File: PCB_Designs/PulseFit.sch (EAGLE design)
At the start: 54 parts

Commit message: updates
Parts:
- removed C10, C9: 100n, resistor:C-EUC0402
- removed COMP, VREF: AD8603UJ, analog-devices:AD8603UJ
- removed JST: JST-PTH, Orlando:JST-PTH
- removed LED1, LED10, LED12, LED16, LED2, LED22, LED23, LED24, LED25, LED26, LED28, LED3, LED4, LED6, LED7, LED8, LED9: (no value), SparkFun-LED:LED5MM
- removed PD1, PD2: PD-ODD-900-001, Orlando:PD-ODD-900-001
- removed R6, R7: 49.9k, resistor:R-US_R0402
- added BATT-CR2032: (no value), SparkFun-Electromechanical:BATTERY20SMD
- added C11: 10n, resistor:C-EUC0402
- added LD1, LD10, LD12, LD13, LD14, LD15, LD16, LD17, LD18, LD2, LD3, LD4, LD5, LD6, LD7, LD8, LD9, LED13: LED-LTST-C230KRKT, Orlando:LED-LTST-C230KRKT
- added PD: LED-PD15-22B_TR8, Orlando:LED-PD15-22B_TR8
- C1: value 33n -> 1uF
- C2, C4: value 570n -> 1u
- C3: value 318n -> 10u; device resistor:C-EUC0402 -> resistor:C-EUC0805
- C5: value 318n -> 10n
- C6: device resistor:C-EUC0402 -> resistor:C-EUC0805
- C7: value 100n -> 10n
- C8: value 100n -> 10u; device resistor:C-EUC0402 -> resistor:C-EUC0805
- GAIN: value AD8609RU -> MCP6004
- LED11: value (none) -> LED-LTST-C230KRKT; device SparkFun-LED:LED5MM -> Orlando:LED-LTST-C230KRKT
- POWER: value ON -> SWITCH-DPDT-JS202011JCQN; device SparkFun-LED:LED0603 -> SparkFun-Electromechanical:SWITCH-DPDT-JS202011JCQN
- R1: value 1M -> 32k
- R10: value 100k -> 3.3M
- R11, R5: value 10k -> 32k
- R13: value (none) -> 169
- R14: value 100 -> 1k
- R2: value 1M -> 3.3M
- R3, R8, R9: value 1M -> 1.5M
- R4: value 100k -> 1.5M
- renumbered LED5 to PULSE
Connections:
- removed net 1/2-VDD: R11.1, R5.1, VREF.IN-, VREF.OUT
- removed net N$7: R6.1, R7.2, VREF.IN+
- new net N$11: C11.2, C4.1, GAINB.OUT, R2.2
- new net N$14: C8.2, R5.1
- net ANODE: now also LD1.A, LD10.A, LD12.A, LD13.A, LD14.A, LD15.A, LD16.A, LD17.A, LD18.A, LD2.A, LD3.A, LD4.A, LD5.A, LD6.A, LD7.A, LD8.A, LD9.A; no longer LED1.A, LED10.A, LED12.A, LED16.A, LED2.A, LED22.A, LED23.A, LED24.A, LED25.A, LED26.A, LED28.A, LED3.A, LED4.A, LED6.A, LED7.A, LED8.A, LED9.A
- net COMP: now also BREAKOUT.3, GAIND.OUT; no longer BREAKOUT.1, COMP.OUT
- net GND: now also BATT-CR2032.-, C3.1, C8.1, LD1.C, LD10.C, LD12.C, LD13.C, LD14.C, LD15.C, LD16.C, LD17.C, LD18.C, LD2.C, LD3.C, LD4.C, LD5.C, LD6.C, LD7.C, LD8.C, LD9.C, POWER.4, POWER.5, POWER.6, R4.2; no longer C10.2, C8.2, C9.2, COMP.-VS, GAINA.IN+, JST.-, LED1.C, LED10.C, LED12.C, LED16.C, LED2.C, LED22.C, LED23.C, LED24.C, LED25.C, LED26.C, LED28.C, LED3.C, LED4.C, LED6.C, LED7.C, LED8.C, LED9.C, PD1.+, PD2.+, R3.2, R6.2, VREF.-VS
- net N$1: now also PD.A; no longer PD1.-, PD2.-
- net N$10: now also C11.1, GAINB.IN-, R2.1, R5.2; no longer D1.A, GAIND.IN-, GAIND.OUT
- net N$12: now also LED13.C; no longer POWER.C
- net N$4: now also R3.2, R4.1; no longer R2.2, R3.1
- net N$5: now also BATT-CR2032.+, POWER.2; no longer C3.1, GAINB.IN-, R4.1, R5.2
- net N$6: now also R11.1; no longer C4.1, GAINB.OUT, R4.2
- net PEAK: now also GAIND.IN-; no longer COMP.IN-
- net PULSE: now also BREAKOUT.1, D1.A; no longer BREAKOUT.3, COMP.IN+
- net VCC: now also GAINA.IN+, LED13.A, PD.C, POWER.1, R3.1; no longer C10.1, C8.1, C9.1, COMP.+VS, JST.+, POWER.A, R2.1, R7.1, VREF.+VS
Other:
- note added: "Orlando S. Hoilett @oshoilett @CalvaryEngineering Made in the @IICEPD Creative Commons License Attribution-NonCommercial- ShareAlike 3.0 Unported"
- note added: "PulseFit V.4.0"
- note added: "Threshold Adjuster and Pulse Detector"
- note removed: "1/2 Vcc Generator"
- note removed: "Orlando S. Hoilett Calvary Eng, IICEPD Creative Commons License Attribution-NonCommercial-ShareAlike"
- note removed: "Pulse Detector"
- note removed: "PulseFit V.1.0"
- note removed: "Threshold Adjuster"
- moved on the sheet: BREAKOUT, C2, C3, C4, C6, C7, C8, D1, GAINB, GAIND, GAINP, LED11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

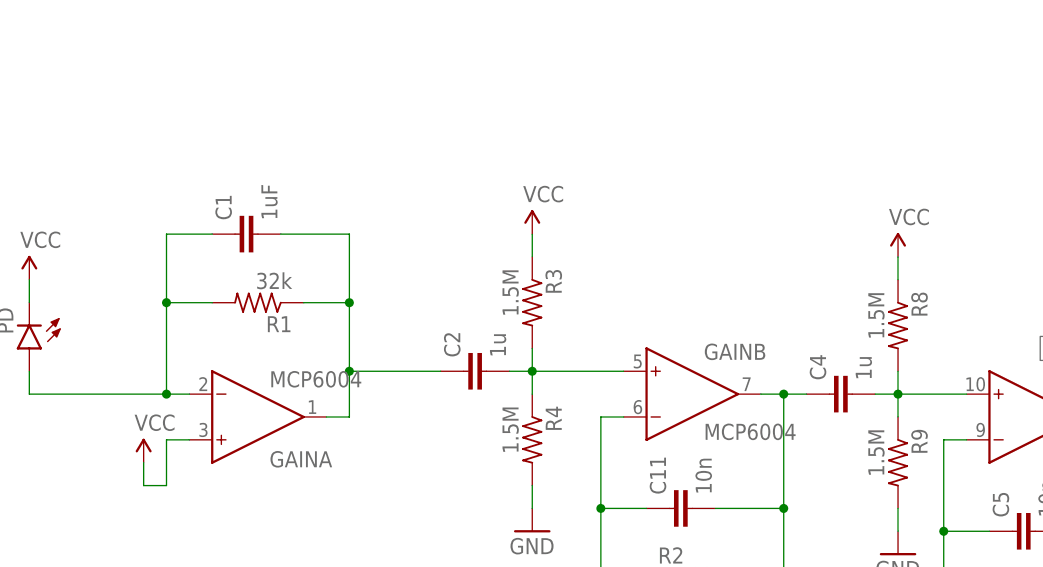
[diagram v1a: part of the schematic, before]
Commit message: updated PulseFit BOM and added disclaimer in schematic
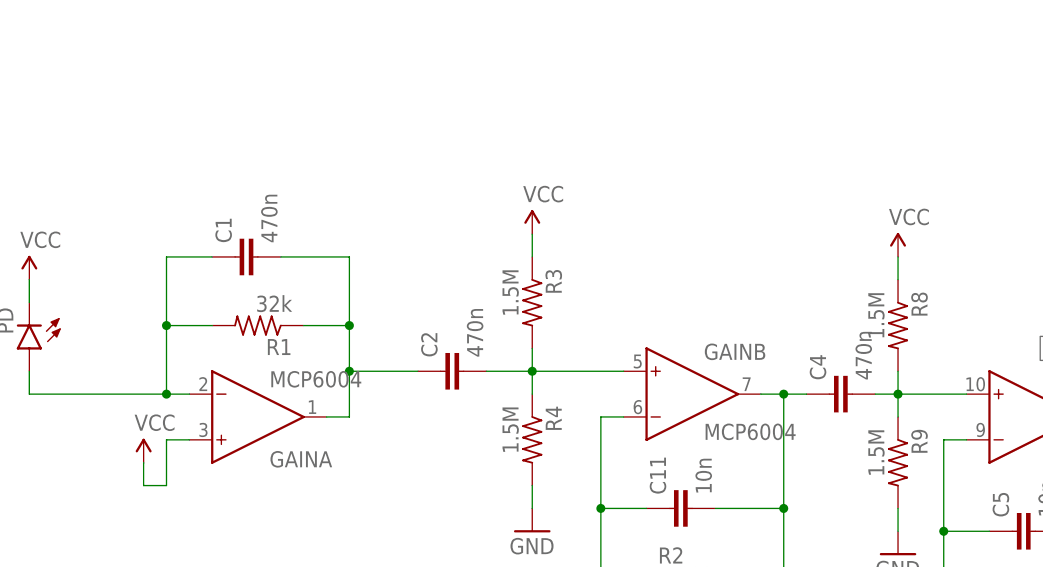
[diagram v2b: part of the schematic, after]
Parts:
- C1: value 1uF -> 470n
- C2, C4: value 1u -> 470n
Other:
- note added: "NOTE: This is NOT a medical device"
- note added: "Orlando S. Hoilett @oshoilett @CalvaryEngineering Made in the @IICEPD Creative Commons License Attribution-NonCommercial- ShareAlike 4.0 Unported"
- note removed: "Orlando S. Hoilett @oshoilett @CalvaryEngineering Made in the @IICEPD Creative Commons License Attribution-NonCommercial- ShareAlike 3.0 Unported"
- moved on the sheet: C1, C2, R1
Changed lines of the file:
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@@
 <?xml version="1.0" encoding="utf-8"?>
 <!DOCTYPE eagle SYSTEM "eagle.dtd">
-<eagle version="7.4.0">
+<eagle version="7.3.0">
 <drawing>
 <settings>
@@
 <parts>
 <part name="GAIN" library="analog-devices" deviceset="AD8609" device="RU" value="MCP6004"/>
-<part name="C1" library="resistor" deviceset="C-EU" device="C0402" value="1uF"/>
+<part name="C1" library="resistor" deviceset="C-EU" device="C0402" value="470n"/>
 <part name="R1" library="resistor" deviceset="R-US_" device="R0402" value="32k"/>
-<part name="C4" library="resistor" deviceset="C-EU" device="C0402" value="1u"/>
+<part name="C4" library="resistor" deviceset="C-EU" device="C0402" value="470n"/>
 <part name="R8" library="resistor" deviceset="R-US_" device="R0402" value="1.5M"/>
 <part name="R9" library="resistor" deviceset="R-US_" device="R0402" value="1.5M"/>
@@
 <part name="C3" library="resistor" deviceset="C-EU" device="C0805" value="10u"/>
 <part name="GND1" library="SparkFun-Aesthetics" deviceset="GND" device=""/>
-<part name="C2" library="resistor" deviceset="C-EU" device="C0402" value="1u"/>
+<part name="C2" library="resistor" deviceset="C-EU" device="C0402" value="470n"/>
 <part name="R3" library="resistor" deviceset="R-US_" device="R0402" value="1.5M"/>
 <part name="R4" library="resistor" deviceset="R-US_" device="R0402" value="1.5M"/>
@@
 Creative Commons License
 Attribution-NonCommercial-
-ShareAlike 3.0 Unported </text>
+ShareAlike 4.0 Unported </text>
 <wire x1="-30.48" y1="147.32" x2="345.44" y2="147.32" width="1.27" layer="94" style="longdash"/>
 <wire x1="345.44" y1="147.32" x2="345.44" y2="-20.32" width="1.27" layer="94" style="longdash"/>
@@
 <wire x1="193.04" y1="88.9" x2="193.04" y2="48.26" width="0.508" layer="90" style="shortdash"/>
 <wire x1="193.04" y1="48.26" x2="139.7" y2="48.26" width="0.508" layer="90" style="shortdash"/>
+<text x="200.66" y="139.7" size="3.81" layer="90">NOTE: This is NOT a medical device</text>
 </plain>
 <instances>
@@
 <instance part="GAIN" gate="D" x="167.64" y="81.28"/>
 <instance part="GAIN" gate="P" x="35.56" y="10.16"/>
-<instance part="C1" gate="G$1" x="35.56" y="96.52" rot="R90"/>
-<instance part="R1" gate="G$1" x="38.1" y="88.9" rot="R180"/>
+<instance part="C1" gate="G$1" x="35.56" y="93.98" rot="R90"/>
+<instance part="R1" gate="G$1" x="38.1" y="86.36" rot="R180"/>
 <instance part="C4" gate="G$1" x="101.6" y="78.74" rot="R90"/>
 <instance part="R8" gate="G$1" x="109.22" y="86.36" rot="R270"/>
@@
 <instance part="C3" gate="G$1" x="114.3" y="35.56" rot="R180"/>
 <instance part="GND1" gate="1" x="114.3" y="27.94"/>
-<instance part="C2" gate="G$1" x="60.96" y="81.28" rot="R90"/>
+<instance part="C2" gate="G$1" x="58.42" y="81.28" rot="R90"/>
 <instance part="R3" gate="G$1" x="68.58" y="88.9" rot="R270"/>
 <instance part="R4" gate="G$1" x="68.58" y="73.66" rot="R270"/>
@@
 <pinref part="R1" gate="G$1" pin="2"/>
 <wire x1="27.94" y1="78.74" x2="12.7" y2="78.74" width="0.1524" layer="91"/>
-<wire x1="33.02" y1="88.9" x2="27.94" y2="88.9" width="0.1524" layer="91"/>
-<wire x1="27.94" y1="88.9" x2="27.94" y2="78.74" width="0.1524" layer="91"/>
+<wire x1="33.02" y1="86.36" x2="27.94" y2="86.36" width="0.1524" layer="91"/>
+<wire x1="27.94" y1="86.36" x2="27.94" y2="78.74" width="0.1524" layer="91"/>
 <junction x="27.94" y="78.74"/>
 <pinref part="C1" gate="G$1" pin="1"/>
-<wire x1="33.02" y1="96.52" x2="27.94" y2="96.52" width="0.1524" layer="91"/>
-<wire x1="27.94" y1="96.52" x2="27.94" y2="88.9" width="0.1524" layer="91"/>
-<junction x="27.94" y="88.9"/>
+<wire x1="33.02" y1="93.98" x2="27.94" y2="93.98" width="0.1524" layer="91"/>
+<wire x1="27.94" y1="93.98" x2="27.94" y2="86.36" width="0.1524" layer="91"/>
+<junction x="27.94" y="86.36"/>
 <wire x1="12.7" y1="81.28" x2="12.7" y2="78.74" width="0.1524" layer="91"/>
 <pinref part="PD" gate="G$1" pin="A"/>
@@
 <segment>
 <pinref part="R1" gate="G$1" pin="1"/>
-<wire x1="43.18" y1="88.9" x2="48.26" y2="88.9" width="0.1524" layer="91"/>
-<wire x1="48.26" y1="88.9" x2="48.26" y2="81.28" width="0.1524" layer="91"/>
+<wire x1="43.18" y1="86.36" x2="48.26" y2="86.36" width="0.1524" layer="91"/>
+<wire x1="48.26" y1="86.36" x2="48.26" y2="81.28" width="0.1524" layer="91"/>
 <pinref part="GAIN" gate="A" pin="OUT"/>
 <wire x1="48.26" y1="81.28" x2="48.26" y2="76.2" width="0.1524" layer="91"/>
 <wire x1="48.26" y1="76.2" x2="45.72" y2="76.2" width="0.1524" layer="91"/>
 <pinref part="C1" gate="G$1" pin="2"/>
-<wire x1="40.64" y1="96.52" x2="48.26" y2="96.52" width="0.1524" layer="91"/>
-<wire x1="48.26" y1="96.52" x2="48.26" y2="88.9" width="0.1524" layer="91"/>
-<junction x="48.26" y="88.9"/>
+<wire x1="40.64" y1="93.98" x2="48.26" y2="93.98" width="0.1524" layer="91"/>
+<wire x1="48.26" y1="93.98" x2="48.26" y2="86.36" width="0.1524" layer="91"/>
+<junction x="48.26" y="86.36"/>
 <junction x="48.26" y="81.28"/>
 <pinref part="C2" gate="G$1" pin="1"/>
-<wire x1="58.42" y1="81.28" x2="48.26" y2="81.28" width="0.1524" layer="91"/>
+<wire x1="55.88" y1="81.28" x2="48.26" y2="81.28" width="0.1524" layer="91"/>
 </segment>
 </net>
@@
 <pinref part="C2" gate="G$1" pin="2"/>
 <pinref part="R3" gate="G$1" pin="2"/>
-<wire x1="66.04" y1="81.28" x2="68.58" y2="81.28" width="0.1524" layer="91"/>
+<wire x1="63.5" y1="81.28" x2="68.58" y2="81.28" width="0.1524" layer="91"/>
 <wire x1="68.58" y1="81.28" x2="68.58" y2="83.82" width="0.1524" layer="91"/>
 <pinref part="R4" gate="G$1" pin="1"/>
